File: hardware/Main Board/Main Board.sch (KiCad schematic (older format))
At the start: 29 parts, among them J1 Motor Power, J2 DEC Motor, J3 RA Motor, J4 Conn_01x05_Female, P1 Conn_02x20_Odd_Even, Q1 2N3904, Q2 2N3904, Q3 2N3904, Q4 2N3904, Q5 2N3904, U1 ELEGOO, U2 ELEGOO

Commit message: First Routing...
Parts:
- removed J4: Conn_01x05_Female, Connector_JST:JST_PH_B5B-PH-K_1x05_P2.00mm_Vertical, symbol Connector:Conn_01x05_Female
- removed Q1, Q2, Q3, Q4, Q5: 2N3904, Package_TO_SOT_THT:TO-92_Inline, symbol Transistor_BJT:2N3904
- removed R1, R10, R11, R12, R2, R3, R4, R7, R8, R9: 100K, Resistor_THT:R_Axial_DIN0204_L3.6mm_D1.6mm_P1.90mm_Vertical, symbol Device:R
- removed R5, R6: 22K, Resistor_THT:R_Axial_DIN0204_L3.6mm_D1.6mm_P1.90mm_Vertical, symbol Device:R
- added J6: System Debug, Connector_PinHeader_1.27mm:PinHeader_1x03_P1.27mm_Vertical, symbol Connector:Conn_01x03_Male
- added J7: DEC Debug, Connector_PinHeader_1.27mm:PinHeader_1x05_P1.27mm_Vertical, symbol Connector:Conn_01x05_Male
- added J8: RA Debug, Connector_PinHeader_1.27mm:PinHeader_1x05_P1.27mm_Vertical, symbol Connector:Conn_01x05_Male
- U1: value ELEGOO -> RA Driver
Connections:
- wire segments 142 -> 148
- no-connect marks 29 -> 27
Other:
- moved on the sheet: C1, J1, J2, J3, P1, U1, U2

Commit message: Extended the Size of the Board
Include space for the DC to DC converters and
re-route.
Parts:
- removed J1: Motor Power, Connector_JST:JST_PH_B2B-PH-K_1x02_P2.00mm_Vertical, symbol Connector:Conn_01x02_Female
- removed J6: System Debug, Connector_PinHeader_1.27mm:PinHeader_1x03_P1.27mm_Vertical, symbol Connector:Conn_01x03_Male
- removed J7: DEC Debug, Connector_PinHeader_1.27mm:PinHeader_1x05_P1.27mm_Vertical, symbol Connector:Conn_01x05_Male
- removed J8: RA Debug, Connector_PinHeader_1.27mm:PinHeader_1x05_P1.27mm_Vertical, symbol Connector:Conn_01x05_Male
- added J3: Battery, Connector_JST:JST_PH_B2B-PH-K_1x02_P2.00mm_Vertical, symbol Connector:Conn_01x02_Female
- added U3, U4: BuckConverter, pimount:BuckConverter, symbol pimount:BuckConverter
- renumbered J2 to J1, J3 to J2, U2 to U1, U1 to U2
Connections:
- net labels added: +6V
- wire segments 148 -> 131
- no-connect marks 27 -> 26

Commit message: merge... main board sch
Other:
- note added: "RJ10\nPin 1 goes to 1A\nPin 2 goes to 2B\nPin 3 goes to 2A\nPin 4 goes to 1B"
- note added: "RJ9\nPin 1 goes to 1A\nPin 2 goes to 2B\nPin 3 goes to 2A\nPin 4 goes to 1B"
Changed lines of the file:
@@
 Wire Wire Line
 	5450 3700 7000 3700
+Text Notes 1200 2350 0    50   ~ 0
+RJ9\nPin 1 goes to 1A\nPin 2 goes to 2B\nPin 3 goes to 2A\nPin 4 goes to 1B
+Text Notes 1200 3600 0    50   ~ 0
+RJ10\nPin 1 goes to 1A\nPin 2 goes to 2B\nPin 3 goes to 2A\nPin 4 goes to 1B
 $EndSCHEMATC

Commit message: Update the Circuit
Move the input on BCM 0 to BCM 12 since BCM 0 and BCM 1
are "special" (the "hat" standard requires and prom there).
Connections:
- net GPIO13(PWM1): now also U2.5 (~RST)
- net GPIO4(GCLK): now also U1.5 (~RST)
- net +6V renamed +10V
- no-connect marks 26 -> 24
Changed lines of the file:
@@
 GPIO2(SDA1)
 Wire Wire Line
-	7500 3400 8550 3400
+	7500 3400 7650 3400
 Wire Wire Line
 	7500 2400 8550 2400
@@
 NoConn ~ 5250 1900
 NoConn ~ 5250 2200
-NoConn ~ 5250 2300
 NoConn ~ 5250 3200
 NoConn ~ 5250 3500
-NoConn ~ 5250 3600
 $Sheet
 S 4750 5700 850  800
@@
 	6050 6300 5600 6300
 Wire Wire Line
-	5650 3200 5650 4750
-Wire Wire Line
-	5650 4750 6150 4750
-Wire Wire Line
-	5650 3200 7000 3200
-Wire Wire Line
 	5600 6400 6150 6400
 Wire Wire Line
@@
 Wire Wire Line
 	8500 5200 8750 5200
-$Comp
-L power:+6V #PWR012
-U 1 1 5D09F8F7
-P 8900 3800
-F 0 "#PWR012" H 8900 3650 50  0001 C CNN
-F 1 "+6V" H 8915 3973 50  0000 C CNN
-F 2 "" H 8900 3800 50  0001 C CNN
-F 3 "" H 8900 3800 50  0001 C CNN
-	1    8900 3800
-	1    0    0    -1
-$EndComp
 Wire Wire Line
 	8900 3800 8900 4000
@@
 	3000 5000 3000 5200
 Connection ~ 3000 5000
-$Comp
-L power:+6V #PWR01
-U 1 1 5D0BF801
-P 3000 4500
-F 0 "#PWR01" H 3000 4350 50  0001 C CNN
-F 1 "+6V" H 3015 4673 50  0000 C CNN
-F 2 "" H 3000 4500 50  0001 C CNN
-F 3 "" H 3000 4500 50  0001 C CNN
-	1    3000 4500
-	1    0    0    -1
-$EndComp
 Wire Wire Line
 	3000 4500 3000 4700
@@
 	5400 2400 5250 2400
 Wire Wire Line
-	5400 2200 5400 2400
+	5400 2200 5400 2300
 Wire Wire Line
 	5250 2100 7000 2100
@@
 	5250 3700 5350 3700
 Wire Wire Line
-	5350 3700 5350 3500
+	5350 3700 5350 3600
 Wire Wire Line
 	5350 3500 7000 3500
@@
 Text Notes 1200 3600 0    50   ~ 0
 RJ10\nPin 1 goes to 1A\nPin 2 goes to 2B\nPin 3 goes to 2A\nPin 4 goes to 1B
+Wire Wire Line
+	5250 3600 5350 3600
+Connection ~ 5350 3600
+Wire Wire Line
+	5350 3600 5350 3500
+Wire Wire Line
+	5250 2300 5400 2300
+Connection ~ 5400 2300
+Wire Wire Line
+	5400 2300 5400 2400
+Wire Wire Line
+	5850 3200 7000 3200
+Wire Wire Line
+	7650 3400 7650 4750
+Wire Wire Line
+	7650 4750 6150 4750
+Connection ~ 7650 3400
+Wire Wire Line
+	7650 3400 8550 3400
+$Comp
+L power:+10V #PWR?
+U 1 1 5D25EF9D
+P 8900 3800
+F 0 "#PWR?" H 8900 3650 50  0001 C CNN
+F 1 "+10V" H 8915 3973 50  0000 C CNN
+F 2 "" H 8900 3800 50  0001 C CNN
+F 3 "" H 8900 3800 50  0001 C CNN
+	1    8900 3800
+	1    0    0    -1
+$EndComp
+$Comp
+L power:+10V #PWR?
+U 1 1 5D25F09C
+P 3000 4500
+F 0 "#PWR?" H 3000 4350 50  0001 C CNN
+F 1 "+10V" H 3015 4673 50  0000 C CNN
+F 2 "" H 3000 4500 50  0001 C CNN
+F 3 "" H 3000 4500 50  0001 C CNN
+	1    3000 4500
+	1    0    0    -1
+$EndComp
 $EndSCHEMATC

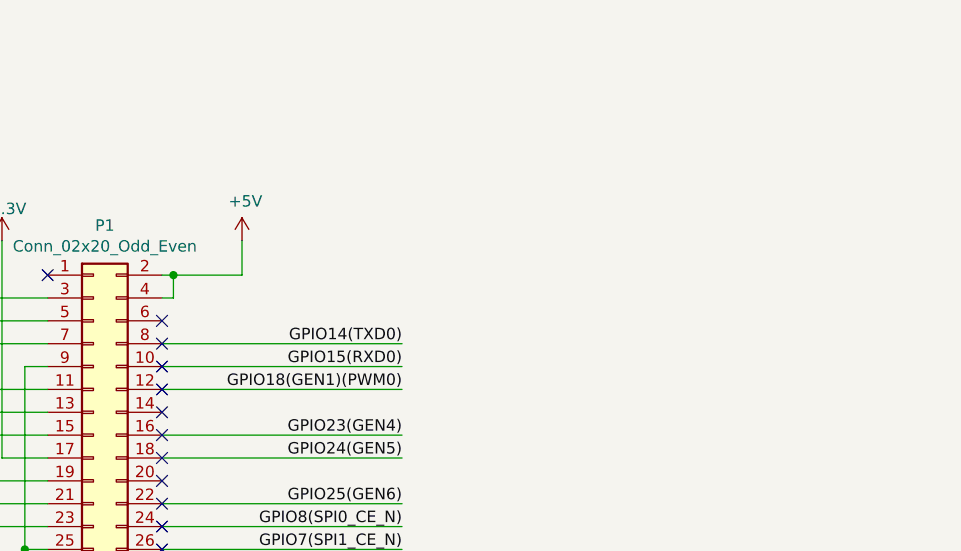
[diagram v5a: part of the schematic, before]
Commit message: Add a Fan Control Circuit
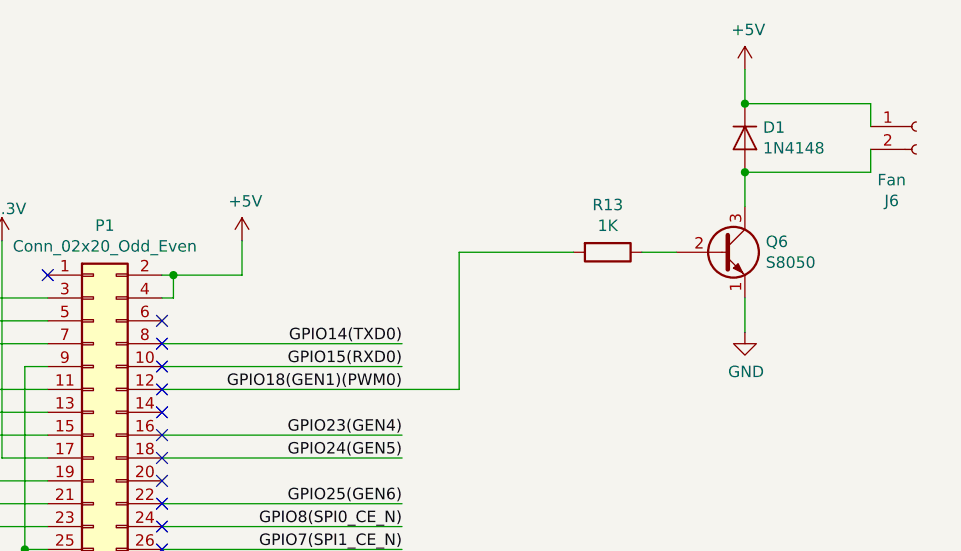
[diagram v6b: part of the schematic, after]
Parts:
- added D1: 1N4148, Diode_THT:D_DO-35_SOD27_P2.54mm_Vertical_KathodeUp, symbol Diode:1N4148
- added J6: Fan, Connector_JST:JST_PH_B2B-PH-K_1x02_P2.00mm_Vertical, symbol Connector:Conn_01x02_Female
- added Q6: S8050, Package_TO_SOT_THT:TO-92_Inline, symbol Transistor_BJT:S8050
- added R13: 1K, Resistor_THT:R_Axial_DIN0204_L3.6mm_D1.6mm_P1.90mm_Vertical, symbol Device:R
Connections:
- net +5V: now also D1.1 (K), J6.1 (Pin_1)
- net GND: now also Q6.1 (E)
- net GPIO18(GEN1)(PWM0): now also R13.2
- new net: D1.2 (A), J6.2 (Pin_2), Q6.3 (C)
- new net: Q6.2 (B), R13.1
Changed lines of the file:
@@
 	7500 3400 7650 3400
-Wire Wire Line
-	7500 2400 8550 2400
 Wire Wire Line
 	7500 2700 8550 2700
@@
 	7650 3400 8550 3400
 $Comp
-L power:+10V #PWR?
+L power:+10V #PWR012
 U 1 1 5D25EF9D
 P 8900 3800
-F 0 "#PWR?" H 8900 3650 50  0001 C CNN
+F 0 "#PWR012" H 8900 3650 50  0001 C CNN
 F 1 "+10V" H 8915 3973 50  0000 C CNN
 F 2 "" H 8900 3800 50  0001 C CNN
@@
 $EndComp
 $Comp
-L power:+10V #PWR?
+L power:+10V #PWR01
 U 1 1 5D25F09C
 P 3000 4500
-F 0 "#PWR?" H 3000 4350 50  0001 C CNN
+F 0 "#PWR01" H 3000 4350 50  0001 C CNN
 F 1 "+10V" H 3015 4673 50  0000 C CNN
 F 2 "" H 3000 4500 50  0001 C CNN
@@
 	1    0    0    -1
 $EndComp
+$Comp
+L Connector:Conn_01x02_Female J6
+U 1 1 5D25F838
+P 10800 1250
+F 0 "J6" H 10692 925 50  0000 C CNN
+F 1 "Fan" H 10692 1016 50  0000 C CNN
+F 2 "Connector_JST:JST_PH_B2B-PH-K_1x02_P2.00mm_Vertical" H 10800 1250 50  0001 C CNN
+F 3 "~" H 10800 1250 50  0001 C CNN
+	1    10800 1250
+	1    0    0    -1
+$EndComp
+$Comp
+L Transistor_BJT:S8050 Q6
+U 1 1 5D25FF21
+P 9950 1800
+F 0 "Q6" H 10141 1846 50  0000 L CNN
+F 1 "S8050" H 10141 1755 50  0000 L CNN
+F 2 "Package_TO_SOT_THT:TO-92_Inline" H 10150 1725 50  0001 L CIN
+F 3 "http://www.unisonic.com.tw/datasheet/S8050.pdf" H 9950 1800 50  0001 L CNN
+	1    9950 1800
+	1    0    0    -1
+$EndComp
+$Comp
+L Diode:1N4148 D1
+U 1 1 5D260018
+P 10050 1300
+F 0 "D1" V 10004 1379 50  0000 L CNN
+F 1 "1N4148" V 10095 1379 50  0000 L CNN
+F 2 "Diode_THT:D_DO-35_SOD27_P2.54mm_Vertical_KathodeUp" H 10050 1125 50  0001 C CNN
+F 3 "http://www.nxp.com/documents/data_sheet/1N4148_1N4448.pdf" H 10050 1300 50  0001 C CNN
+	1    10050 1300
+	0    1    1    0
+$EndComp
+$Comp
+L Device:R R13
+U 1 1 5D2600A5
+P 9450 1800
+F 0 "R13" V 9243 1800 50  0000 C CNN
+F 1 "1K" V 9334 1800 50  0000 C CNN
+F 2 "Resistor_THT:R_Axial_DIN0204_L3.6mm_D1.6mm_P1.90mm_Vertical" V 9380 1800 50  0001 C CNN
+F 3 "~" H 9450 1800 50  0001 C CNN
+	1    9450 1800
+	0    1    1    0
+$EndComp
+$Comp
+L power:+5V #PWR016
+U 1 1 5D265707
+P 10050 1000
+F 0 "#PWR016" H 10050 850 50  0001 C CNN
+F 1 "+5V" H 10065 1173 50  0000 C CNN
+F 2 "" H 10050 1000 50  0001 C CNN
+F 3 "" H 10050 1000 50  0001 C CNN
+	1    10050 1000
+	1    0    0    -1
+$EndComp
+Wire Wire Line
+	10050 1000 10050 1150
+Wire Wire Line
+	10050 1150 10600 1150
+Wire Wire Line
+	10600 1150 10600 1250
+Connection ~ 10050 1150
+$Comp
+L power:GND #PWR017
+U 1 1 5D2705BD
+P 10050 2150
+F 0 "#PWR017" H 10050 1900 50  0001 C CNN
+F 1 "GND" H 10055 1977 50  0000 C CNN
+F 2 "" H 10050 2150 50  0001 C CNN
+F 3 "" H 10050 2150 50  0001 C CNN
+	1    10050 2150
+	1    0    0    -1
+$EndComp
+Wire Wire Line
+	10050 1450 10050 1600
+Wire Wire Line
+	10050 2000 10050 2150
+Wire Wire Line
+	10050 1450 10600 1450
+Wire Wire Line
+	10600 1450 10600 1350
+Connection ~ 10050 1450
+Wire Wire Line
+	9600 1800 9750 1800
+Wire Wire Line
+	9300 1800 8800 1800
+Wire Wire Line
+	8800 1800 8800 2400
+Wire Wire Line
+	7500 2400 8800 2400
 $EndSCHEMATC

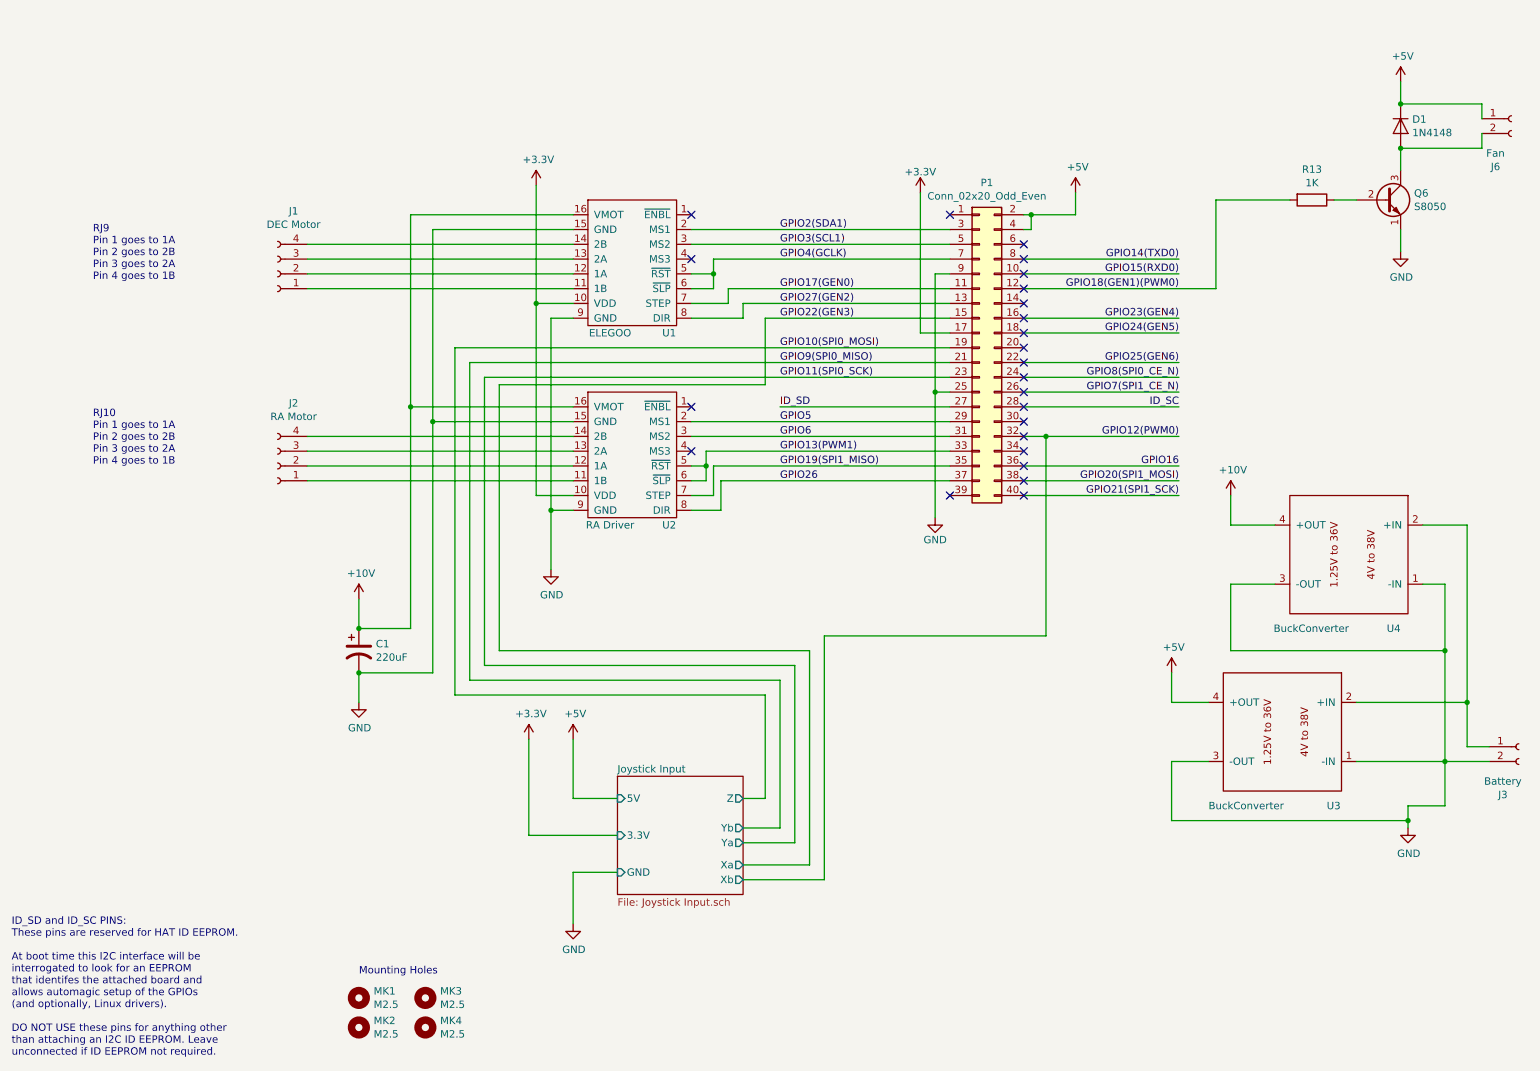
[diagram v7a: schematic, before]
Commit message: Remove the Joystick Circuitry and Cleanup
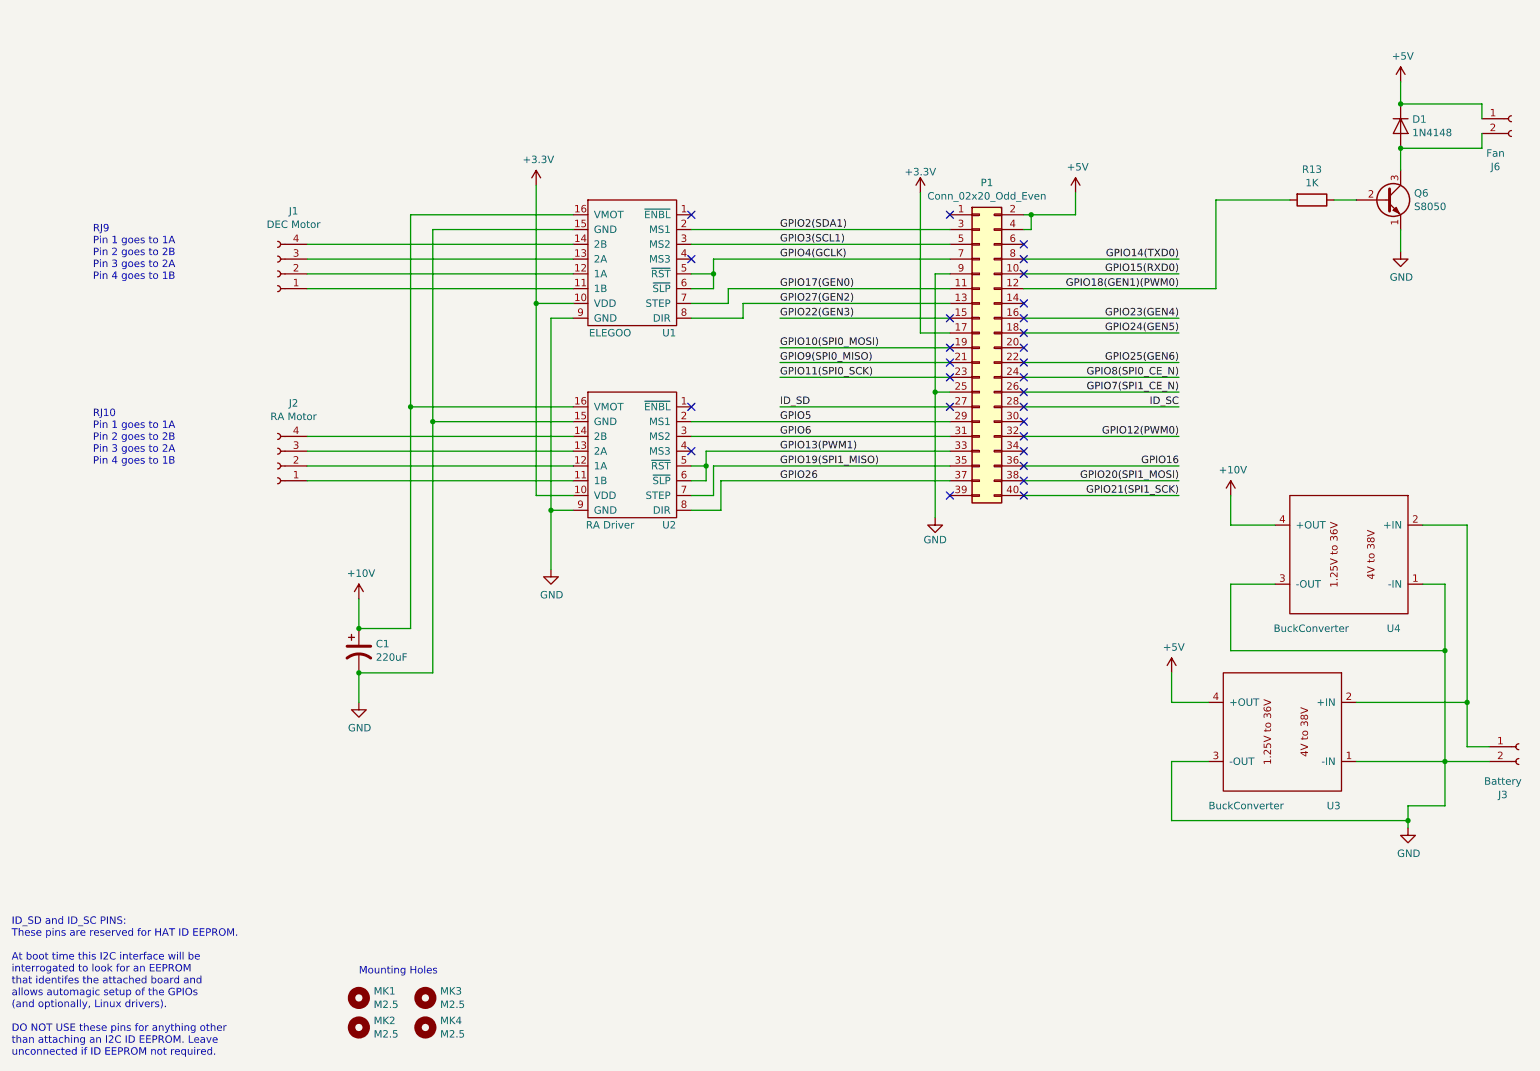
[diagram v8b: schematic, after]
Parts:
- J3: footprint Connector_JST:JST_PH_B2B-PH-K_1x02_P2.00mm_Vertical -> Connector_Phoenix_MC_HighVoltage:PhoenixContact_MCV_1,5_2-G-5.08_1x02_P5.08mm_Vertical
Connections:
- no-connect marks 24 -> 28
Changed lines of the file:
@@
 $Descr A4 11693 8268
 encoding utf-8
-Sheet 1 2
+Sheet 1 1
 Title "pimount"
-Date "2019-07-10"
-Rev "1.2"
+Date "2020-04-22"
+Rev "1.3"
 Comp ""
 Comment1 "https://github.com/eruditelite/pimount.git"
-Comment2 "release_1.2"
+Comment2 "release_1.3"
 Comment3 ""
 Comment4 ""
@@
 Text Label 5850 2900 0    50   ~ 0
 GPIO9(SPI0_MISO)
-Text Label 5850 2800 0    50   ~ 0
-GPIO10(SPI0_MOSI)
 Text Label 5850 2600 0    50   ~ 0
 GPIO22(GEN3)
@@
 GPIO2(SDA1)
 Wire Wire Line
-	7500 3400 7650 3400
-Wire Wire Line
 	7500 2700 8550 2700
 Wire Wire Line
@@
 NoConn ~ 7500 2200
 NoConn ~ 7500 2300
-NoConn ~ 7500 2400
 NoConn ~ 7500 3400
 NoConn ~ 5250 1900
@@
 NoConn ~ 5250 3200
 NoConn ~ 5250 3500
-$Sheet
-S 4750 5700 850  800
-U 5C9A8F22
-F0 "Joystick Input" 50
-F1 "Joystick Input.sch" 50
-F2 "5V" I L 4750 5850 50
-F3 "GND" I L 4750 6350 50
-F4 "3.3V" I L 4750 6100 50
-F5 "Z" O R 5600 5850 50
-F6 "Xa" O R 5600 6300 50
-F7 "Xb" O R 5600 6400 50
-F8 "Ya" O R 5600 6150 50
-F9 "Yb" O R 5600 6050 50
-$EndSheet
-Wire Wire Line
-	4750 6350 4450 6350
-Wire Wire Line
-	4450 6350 4450 6700
-$Comp
-L power:GND #PWR07
-U 1 1 5C9C2D75
-P 4450 6700
-F 0 "#PWR07" H 4450 6450 50  0001 C CNN
-F 1 "GND" H 4455 6527 50  0000 C CNN
-F 2 "" H 4450 6700 50  0001 C CNN
-F 3 "" H 4450 6700 50  0001 C CNN
-	1    4450 6700
-	1    0    0    -1
-$EndComp
-Wire Wire Line
-	4750 5850 4450 5850
-Wire Wire Line
-	4450 5850 4450 5450
-$Comp
-L power:+5V #PWR06
-U 1 1 5C9C5B5C
-P 4450 5450
-F 0 "#PWR06" H 4450 5300 50  0001 C CNN
-F 1 "+5V" H 4465 5623 50  0000 C CNN
-F 2 "" H 4450 5450 50  0001 C CNN
-F 3 "" H 4450 5450 50  0001 C CNN
-	1    4450 5450
-	1    0    0    -1
-$EndComp
-Wire Wire Line
-	4750 6100 4150 6100
-Wire Wire Line
-	4150 6100 4150 5450
-$Comp
-L power:+3.3V #PWR03
-U 1 1 5C9C97CF
-P 4150 5450
-F 0 "#PWR03" H 4150 5300 50  0001 C CNN
-F 1 "+3.3V" H 4165 5623 50  0000 C CNN
-F 2 "" H 4150 5450 50  0001 C CNN
-F 3 "" H 4150 5450 50  0001 C CNN
-	1    4150 5450
-	1    0    0    -1
-$EndComp
-Wire Wire Line
-	3650 2800 3650 5150
-Wire Wire Line
-	3650 5150 5750 5150
-Wire Wire Line
-	5750 5150 5750 5850
-Wire Wire Line
-	5750 5850 5600 5850
-Wire Wire Line
-	3650 2800 7000 2800
-Wire Wire Line
-	7000 2900 3750 2900
-Wire Wire Line
-	3750 2900 3750 5050
-Wire Wire Line
-	3750 5050 5850 5050
-Wire Wire Line
-	5850 5050 5850 6050
-Wire Wire Line
-	5600 6050 5850 6050
-Wire Wire Line
-	3850 4950 5950 4950
-Wire Wire Line
-	5950 4950 5950 6150
-Wire Wire Line
-	5950 6150 5600 6150
-Wire Wire Line
-	3850 3000 7000 3000
-Wire Wire Line
-	3850 3000 3850 4950
 Wire Wire Line
 	7500 2900 8550 2900
-Wire Wire Line
-	5750 2600 5750 3050
-Wire Wire Line
-	5750 3050 3950 3050
-Wire Wire Line
-	3950 3050 3950 4850
-Wire Wire Line
-	3950 4850 6050 4850
-Wire Wire Line
-	6050 4850 6050 6300
-Wire Wire Line
-	6050 6300 5600 6300
-Wire Wire Line
-	5600 6400 6150 6400
-Wire Wire Line
-	6150 4750 6150 6400
 NoConn ~ 7500 2900
-Wire Wire Line
-	5750 2600 7000 2600
 Wire Wire Line
 	7000 3100 6900 3100
@@
 F 0 "J3" H 10742 5175 50  0000 C CNN
 F 1 "Battery" H 10742 5266 50  0000 C CNN
-F 2 "Connector_JST:JST_PH_B2B-PH-K_1x02_P2.00mm_Vertical" H 10850 5500 50  0001 C CNN
+F 2 "Connector_Phoenix_MC_HighVoltage:PhoenixContact_MCV_1,5_2-G-5.08_1x02_P5.08mm_Vertical" H 10850 5500 50  0001 C CNN
 F 3 "~" H 10850 5500 50  0001 C CNN
 	1    10850 5500
@@
 Wire Wire Line
 	5850 3200 7000 3200
-Wire Wire Line
-	7650 3400 7650 4750
-Wire Wire Line
-	7650 4750 6150 4750
-Connection ~ 7650 3400
-Wire Wire Line
-	7650 3400 8550 3400
 $Comp
 L power:+10V #PWR012
@@
 Wire Wire Line
 	7500 2400 8800 2400
+Wire Wire Line
+	5850 2600 7000 2600
+Wire Wire Line
+	5850 2900 7000 2900
+Wire Wire Line
+	5850 3000 7000 3000
+Wire Wire Line
+	7500 3400 8550 3400
+Text Label 5850 2800 0    50   ~ 0
+GPIO10(SPI0_MOSI)
+Wire Wire Line
+	5850 2800 7000 2800
+NoConn ~ 7000 3200
+NoConn ~ 7000 3000
+NoConn ~ 7000 2900
+NoConn ~ 7000 2800
+NoConn ~ 7000 2600
 $EndSCHEMATC
